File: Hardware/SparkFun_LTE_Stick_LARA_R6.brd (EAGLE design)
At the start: 25.4 x 82.5 mm, 120 parts, among them IC1 SN74AVC4T774PW, IC3 SN74AVC4T774PW, J1 NANO_SIM, U1 LARA-R6401, U2 AP7361C-33

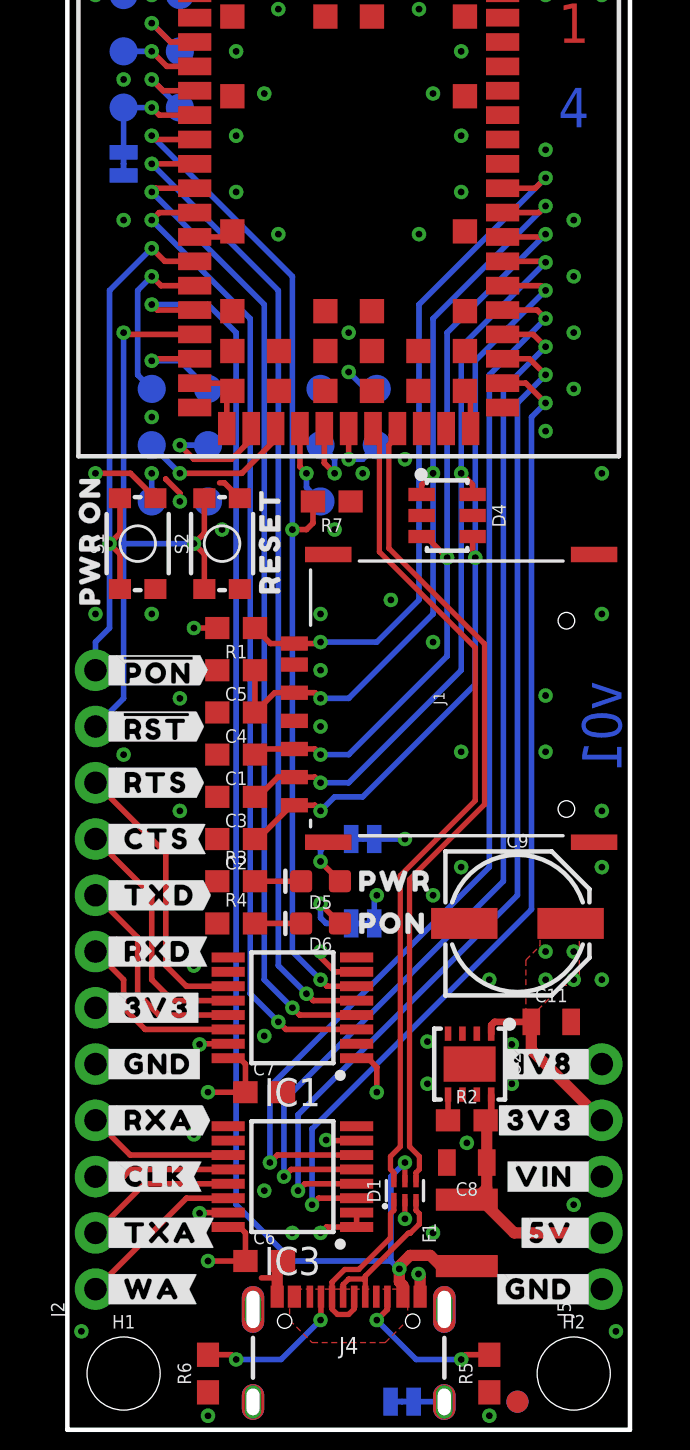
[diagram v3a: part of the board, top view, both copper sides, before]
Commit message: Design Review Updates
Add diodes to PWR_ON and RESET PTH pads to protect against higher voltage inputs
Move R7 to other side of level shifter
Add SIM card outline to bottom silk
Prevent bridging between pads of level shifters
Remove 5V PTH pad
Add dueling diodes to VREG input
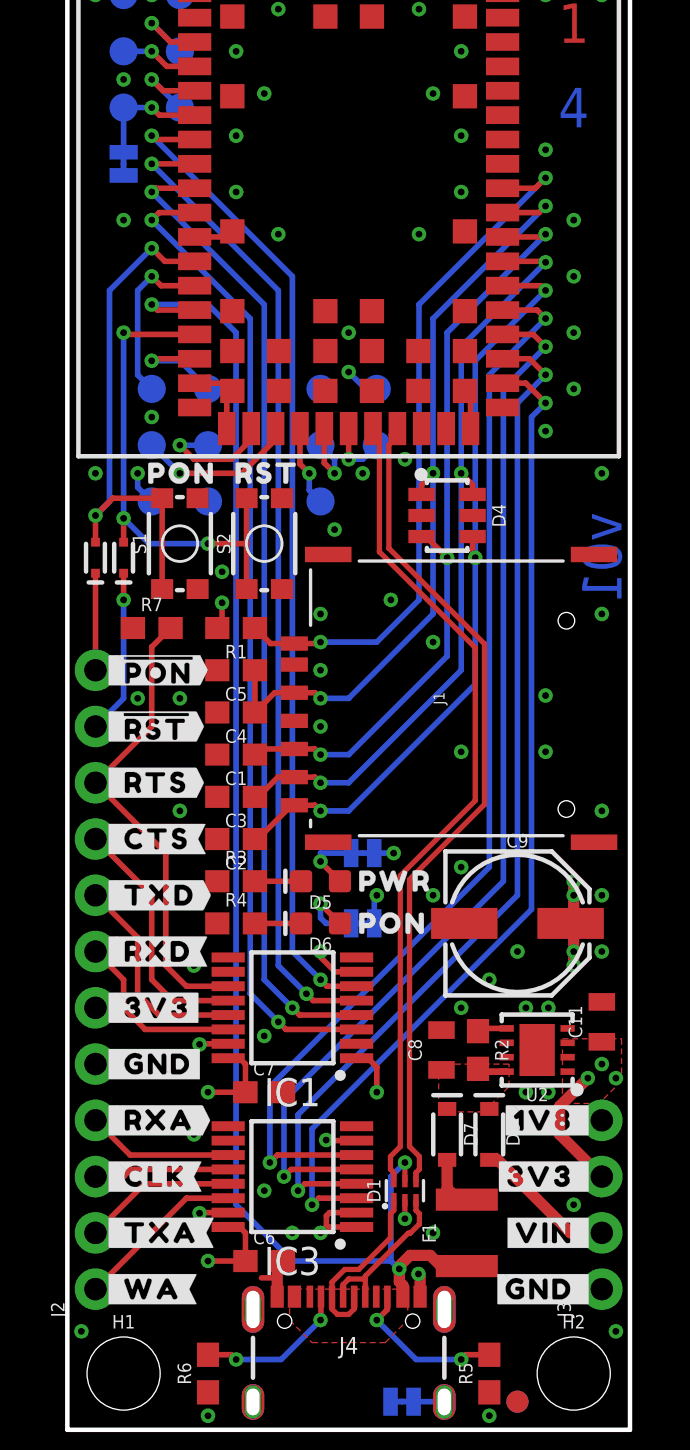
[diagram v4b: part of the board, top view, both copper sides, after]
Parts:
- removed J5: (no value), SparkFun-Connectors:1X05_NO_SILK
- removed U$27: (no value), output:#_5V#0
- removed U$30: (no value), output:RESET0
- removed U$34: (no value), output:PWR_ON0
- added D10, D9: 120mA/40V/370mV, SparkFun-DiscreteSemi:SOD-523
- added D7, D8: 3A/10V/280mV, SparkFun-DiscreteSemi:SOD-323
- added J3: (no value), SparkFun-Connectors:1X04_NO_SILK
- added U$51: (no value), output:ORIENTATION0
- added U$52: (no value), output:RST0
- added U$53: (no value), output:PON0
- U$26: device output:#5V_#0 -> output:SIM_CARD0
- moved U$26 24.0 mm to (19.1, 32.4), flipped to the bottom
- moved R7 9.94 mm to (3.81, 36.2), turned to 0 degrees
- moved C8 5.21 mm to (16.9, 17.1), turned to 90 degrees
- moved R2 3.22 mm to (18.5, 17.1), turned to 270 degrees
- moved U2 3.11 mm to (21.2, 17.1), turned to 90 degrees
- moved U$12 2.54 mm to (23.9, 11.4)
- moved U$13 2.54 mm to (23.9, 14.0)
- moved U$14 2.54 mm to (23.9, 14.0)
- moved U$15 2.54 mm to (23.9, 11.4)
- moved U$11 2.54 mm to (23.9, 8.89)
- moved U$16 2.54 mm to (23.9, 8.89)
- moved C11 2.29 mm to (24.1, 18.4), turned to 90 degrees
- moved S1 1.91 mm to (5.08, 40.0)
- moved S2 1.91 mm to (8.89, 40.0)
- moved PWR 0.64 mm to (13.3, 26.0)
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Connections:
- removed net PWR_ON: J2.12, S1.3, S1.4, U1.15
- new net !PWR_ON!: D9.A, S1.3, S1.4, U1.15
- new net N$5: D10.C, J2.11
- new net N$6: D9.C, J2.12
- new net N$7: C8.1, D7.C, D8.C, R2.2, U2.8
- net !RESET!: now also D10.A; no longer J2.11
- net 1.8V: now also J3.4; no longer J5.5
- net 3.3V: now also J3.3; no longer J5.4
- net 5V: now also D7.A; no longer C8.1, J5.2, R2.2, U2.8
- net GND: now also J3.1; no longer J5.1
- net RTS_18: no longer R7.2
- net RTS_33: now also R7.2
- net VIN: now also D8.A, J3.2; no longer J5.3
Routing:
- net PWR_ON: track 26.8 -> 0.00 mm, vias 2 -> 0
- net !PWR_ON!: track 0.00 -> 23.9 mm, vias 0 -> 2
- net 5V: track 12.2 -> 2.39 mm
- net RTS_33: track 12.8 -> 21.2 mm
- net N$5: track 0.00 -> 7.45 mm, vias 0 -> 1
- net VIN: track 0.00 -> 6.44 mm
- net !RESET!: track 29.2 -> 22.8 mm, vias 2 -> 3
- net GND: track 24.4 -> 18.7 mm, vias 131 -> 129
- net N$6: track 0.00 -> 4.38 mm
- net RTS_18: track 47.0 -> 45.0 mm, vias 3 -> 2
- net 1.8V: track 37.5 -> 39.3 mm
- net N$7: track 0.00 -> 1.34 mm
- net 3.3V: track 12.0 -> 13.2 mm, vias 11 -> 14
- added copper zone on layer 1, net N$7

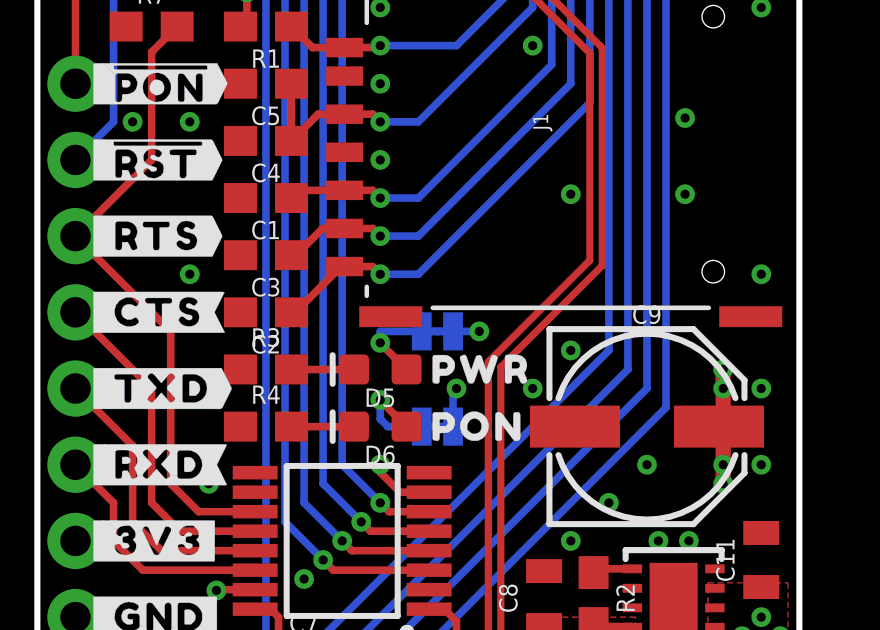
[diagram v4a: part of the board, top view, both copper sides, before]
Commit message: Design Review Updates
Add note to silkscreen about voltage level for PTH pads and test points
Move PWR LED via away from USB trace
Adjust measure for SIM card
Add ordering instructions
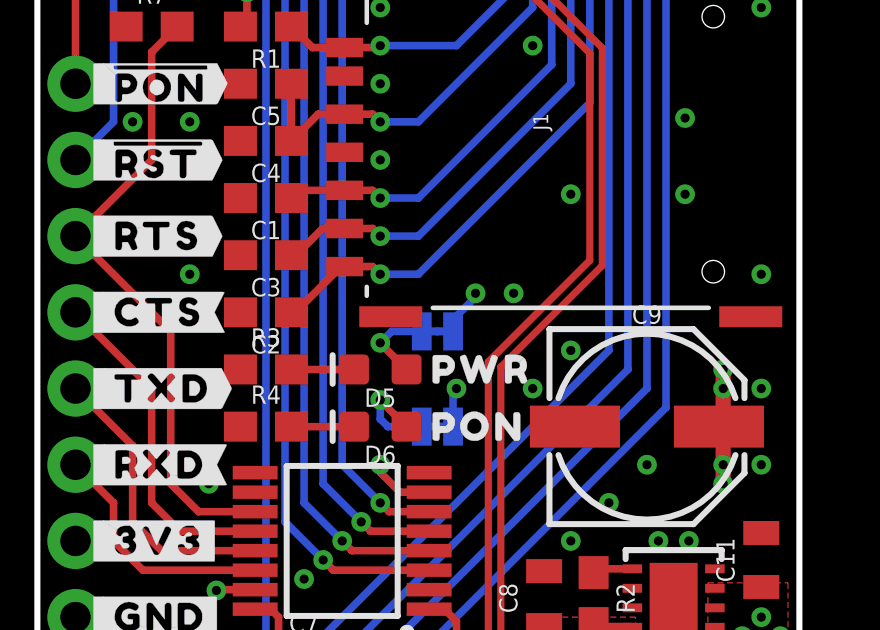
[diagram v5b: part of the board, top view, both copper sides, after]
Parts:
- added U$27: (no value), output:VOLTAGE_LEVEL0
- added U$30: (no value), output:TEST_POINTS0
- added U$34: (no value), output:PTH_PADS0
- added U$50: (no value), output:1#8V0
- added U$54: (no value), output:3#3V0
- added U$55: (no value), SparkFun-Aesthetics:ORDERING_INSTRUCTIONS
- moved LOGO2 26.0 mm to (12.7, 79.4)
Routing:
- net 3.3V: track 13.2 -> 13.9 mm
- net GND: vias 129 -> 130
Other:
- board text added: "4-layer JLC7628 Stackup Material: TG135-140 1oz outer layers 0.5oz inner layers Board thickness: 1.6mm Soldermask: Red Silkscreen: White Surface Finish: Lead-Free HASL"
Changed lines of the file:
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@@
 <dimension x1="25.4" y1="0" x2="25.4" y2="6.35" x3="29.21" y3="3.175" textsize="1.778" textratio="15" layer="47" unit="inch"/>
 <dimension x1="25.4" y1="0" x2="25.4" y2="13.97" x3="33.02" y3="6.985" textsize="1.778" textratio="15" layer="47" unit="inch"/>
-<dimension x1="25.4" y1="0" x2="25.4" y2="31.75" x3="36.83" y3="15.875" textsize="1.778" textratio="15" layer="47" unit="inch"/>
+<dimension x1="25.4" y1="0" x2="25.4" y2="31.877" x3="36.83" y3="15.9385" textsize="1.778" textratio="15" layer="47" unit="inch" precision="3"/>
 <dimension x1="0" y1="82.55" x2="4.445" y2="82.55" x3="2.2225" y3="91.44" textsize="1.778" textratio="15" layer="47" unit="inch" precision="3"/>
 <dimension x1="0" y1="82.55" x2="20.955" y2="82.55" x3="10.4775" y3="95.25" textsize="1.778" textratio="15" layer="47" unit="inch" precision="3"/>
@@
 <wire x1="24.83" y1="35.57" x2="24.141" y2="36.27" width="0.2032" layer="22" curve="90.025014"/>
 <wire x1="24.13" y1="27.47" x2="24.83" y2="28.159" width="0.2032" layer="22" curve="90.025014"/>
+<wire x1="20.32" y1="55.88" x2="20.32" y2="53.34" width="0.254" layer="22"/>
+<wire x1="20.32" y1="53.34" x2="20.32" y2="50.8" width="0.254" layer="22"/>
+<wire x1="20.32" y1="50.8" x2="20.32" y2="48.26" width="0.254" layer="22"/>
+<wire x1="20.32" y1="48.26" x2="10.16" y2="48.26" width="0.254" layer="22"/>
+<wire x1="10.16" y1="48.26" x2="5.08" y2="48.26" width="0.254" layer="22"/>
+<wire x1="5.08" y1="48.26" x2="5.08" y2="50.8" width="0.254" layer="22"/>
+<wire x1="5.08" y1="50.8" x2="5.08" y2="53.34" width="0.254" layer="22"/>
+<wire x1="5.08" y1="53.34" x2="5.08" y2="55.88" width="0.254" layer="22"/>
+<wire x1="5.08" y1="55.88" x2="20.32" y2="55.88" width="0.254" layer="22"/>
+<wire x1="20.32" y1="53.34" x2="10.16" y2="53.34" width="0.254" layer="22"/>
+<wire x1="10.16" y1="53.34" x2="5.08" y2="53.34" width="0.254" layer="22"/>
+<wire x1="20.32" y1="50.8" x2="10.16" y2="50.8" width="0.254" layer="22"/>
+<wire x1="10.16" y1="50.8" x2="5.08" y2="50.8" width="0.254" layer="22"/>
+<wire x1="10.16" y1="53.34" x2="10.16" y2="50.8" width="0.254" layer="22"/>
+<wire x1="10.16" y1="50.8" x2="10.16" y2="48.26" width="0.254" layer="22"/>
+<text x="41.91" y="40.64" size="1.778" layer="51" font="vector" align="top-left">4-layer
+JLC7628 Stackup
+Material: TG135-140
+1oz outer layers
+0.5oz inner layers
+Board thickness: 1.6mm
+Soldermask: Red
+Silkscreen: White
+Surface Finish: Lead-Free HASL</text>
 </plain>
 <attributes>
@@
 </element>
 <element name="U$10" library="output" package="#DTR#0" value="" x="3.175" y="57.15" smashed="yes" rot="MR0"/>
-<element name="LOGO2" library="SparkFun-Aesthetics" package="OSHW-LOGO-M" value="OSHW-LOGOM" x="12.7" y="53.34" smashed="yes" rot="MR0"/>
+<element name="LOGO2" library="SparkFun-Aesthetics" package="OSHW-LOGO-M" value="OSHW-LOGOM" x="12.7" y="79.375" smashed="yes" rot="MR0"/>
 <element name="D5" library="SparkFun-LED" package="LED-0603" value="" x="11.43" y="24.765" smashed="yes" rot="R180">
 <attribute name="NAME" x="11.43" y="24.13" size="0.6096" layer="25" font="vector" ratio="20" rot="R180" align="bottom-center"/>
@@
 </element>
 <element name="U$26" library="output" package="SIM_CARD0" value="" x="19.05" y="32.385" smashed="yes" rot="MR0"/>
+<element name="U$27" library="output" package="VOLTAGE_LEVEL0" value="" x="12.7" y="54.61" smashed="yes" rot="MR0"/>
+<element name="U$30" library="output" package="TEST_POINTS0" value="" x="15.24" y="52.07" smashed="yes" rot="MR0"/>
+<element name="U$34" library="output" package="PTH_PADS0" value="" x="15.24" y="49.53" smashed="yes" rot="MR0"/>
+<element name="U$50" library="output" package="1#8V0" value="" x="7.62" y="52.07" smashed="yes" rot="MR0"/>
+<element name="U$54" library="output" package="3#3V0" value="" x="7.62" y="49.53" smashed="yes" rot="MR0"/>
+<element name="U$55" library="SparkFun-Aesthetics" package="ORDERING_INSTRUCTIONS" value="" x="40.64" y="50.8" smashed="yes"/>
 </elements>
 <signals>
@@
 <via x="19.05" y="20.32" extent="1-16" drill="0.3048"/>
 <via x="20.32" y="21.59" extent="1-16" drill="0.3048"/>
+<via x="15.875" y="27.305" extent="1-16" drill="0.3048"/>
 </signal>
 <signal name="3.3V">
@@
 <contactref element="J2" pad="6"/>
 <contactref element="PWR" pad="2"/>
-<wire x1="13.8557" y1="26.035" x2="14.732" y2="26.035" width="0.254" layer="16"/>
-<via x="14.732" y="26.035" extent="1-16" drill="0.3048"/>
+<wire x1="14.605" y1="27.305" x2="14.605" y2="27.178" width="0.254" layer="16"/>
+<wire x1="14.605" y1="27.178" x2="13.8557" y2="26.4287" width="0.254" layer="16"/>
+<wire x1="13.8557" y1="26.4287" x2="13.8557" y2="26.035" width="0.254" layer="16"/>
+<via x="14.605" y="27.305" extent="1-16" drill="0.3048"/>
 <contactref element="J3" pad="3"/>
 <via x="24.13" y="16.51" extent="1-16" drill="0.3048"/>
@@
 <wire x1="11.43" y1="25.642" x2="11.43" y2="25.654" width="0.254" layer="1"/>
 <via x="11.43" y="25.654" extent="1-16" drill="0.3048"/>
-<wire x1="12.8143" y1="26.035" x2="11.43" y2="26.035" width="0.254" layer="16"/>
-<wire x1="11.43" y1="26.035" x2="11.43" y2="25.654" width="0.254" layer="16"/>
+<wire x1="12.8143" y1="26.035" x2="11.811" y2="26.035" width="0.254" layer="16"/>
+<wire x1="11.811" y1="26.035" x2="11.43" y2="25.654" width="0.254" layer="16"/>
 </signal>
 <signal name="N$3">
@@
 </drawing>
 <compatibility>
+<note version="6.3" minversion="6.2.2" severity="warning">
+Since Version 6.2.2 text objects can contain more than one line,
+which will not be processed correctly with this version.
+</note>
 <note version="8.3" severity="warning">
 Since Version 8.3, EAGLE supports URNs for individual library
